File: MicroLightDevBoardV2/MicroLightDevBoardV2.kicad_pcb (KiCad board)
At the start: 2 copper layers, 80.4 x 72.6 mm, 65 parts, among them J1 Conn_01x05_Socket, J10 Conn_01x01_Socket, J11 Conn_01x05_Socket, J12 Conn_01x02_Socket, J13 Conn_01x04_Socket, J14 Conn_01x04_Socket, J15 Conn_01x05_Socket, J16 Conn_01x01_Socket, J17 Conn_01x04_Socket, J18 Conn_01x04_Socket, J19 Conn_01x04_Socket, J2 Conn_01x05_Socket, J20 Conn_01x04_Socket, J21 Conn_01x04_Socket, J22 Conn_01x04_Socket, J23 Conn_01x03_Socket, J24 Conn_01x03_Socket, J25 Conn_01x04_Socket, J26 Conn_01x04_Socket, J27 Conn_01x02_Socket, J28 Conn_01x02_Socket, J29 Conn_01x02_Socket, J3 Conn_01x05_Socket, J30 Conn_01x02_Socket, J31 Conn_01x01_Socket, J32 Conn_01x06_Socket, J33 Conn_01x04_Socket, J4 Conn_01x05_Socket, J5 Conn_01x02_Socket, J6 Conn_01x02_Socket, J7 TYPE-C-31-M-12, J8 Conn_01x02_Socket, J9 Conn_01x02_Socket, U1 BQ25628RYKR, U2 ATtiny3226-M, U3 S-85S1AB33-I6T1U, U4 USBLC6-2P6, U5 MC3479

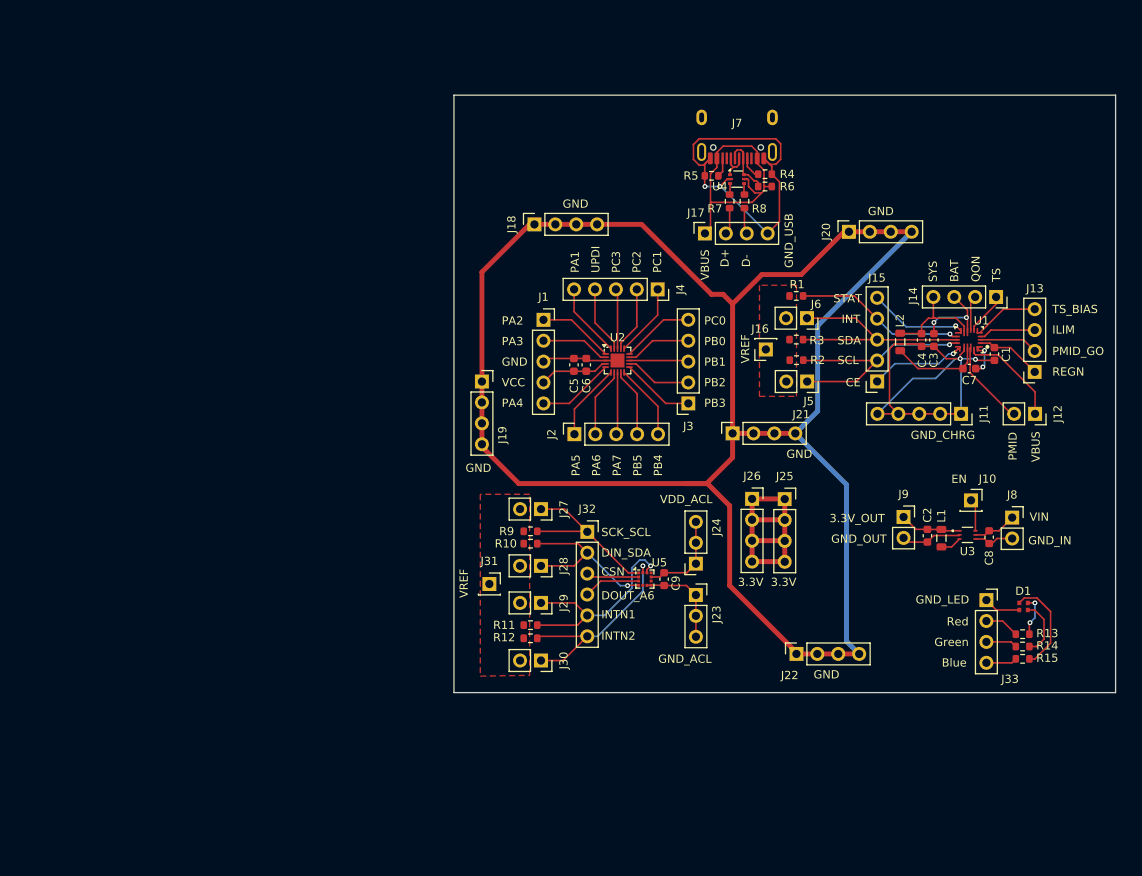
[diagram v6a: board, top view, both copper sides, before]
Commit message: add buttons to pcb, add breadboard like expansion sockets
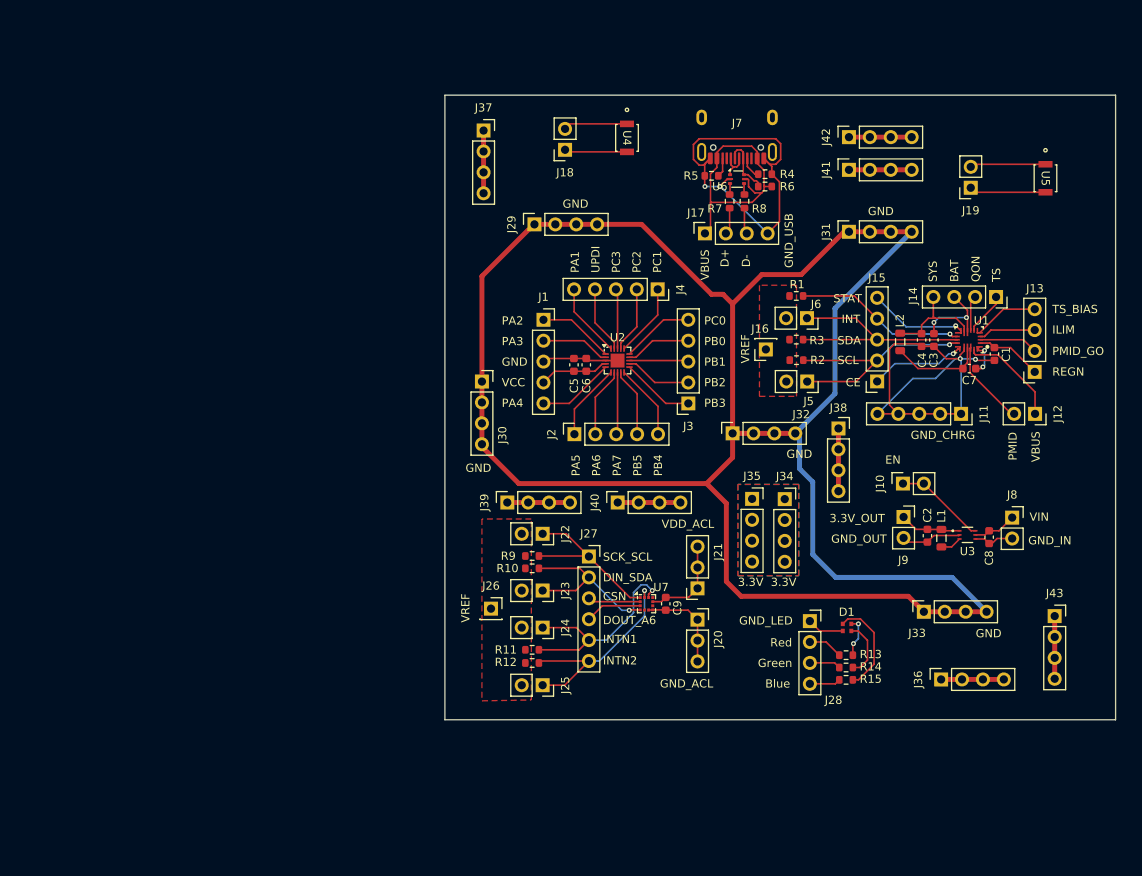
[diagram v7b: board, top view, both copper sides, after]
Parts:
- added J18: Conn_01x02_Socket, Connector_PinSocket_2.54mm:PinSocket_1x02_P2.54mm_Vertical, F.Cu at (132.8, 43.4)
- added J19: Conn_01x02_Socket, Connector_PinSocket_2.54mm:PinSocket_1x02_P2.54mm_Vertical, F.Cu at (182.1, 48.0)
- added J36: Conn_01x04_Socket, Connector_PinSocket_2.54mm:PinSocket_1x04_P2.54mm_Vertical, F.Cu at (178.5, 107.8)
- added J37: Conn_01x04_Socket, Connector_PinSocket_2.54mm:PinSocket_1x04_P2.54mm_Vertical, F.Cu at (122.9, 41.1)
- added J38: Conn_01x04_Socket, Connector_PinSocket_2.54mm:PinSocket_1x04_P2.54mm_Vertical, F.Cu at (166.0, 77.3)
- added J39: Conn_01x04_Socket, Connector_PinSocket_2.54mm:PinSocket_1x04_P2.54mm_Vertical, F.Cu at (125.8, 86.3)
- added J40: Conn_01x04_Socket, Connector_PinSocket_2.54mm:PinSocket_1x04_P2.54mm_Vertical, F.Cu at (139.2, 86.3)
- added J41: Conn_01x04_Socket, Connector_PinSocket_2.54mm:PinSocket_1x04_P2.54mm_Vertical, F.Cu at (167.3, 45.9)
- added J42: Conn_01x04_Socket, Connector_PinSocket_2.54mm:PinSocket_1x04_P2.54mm_Vertical, F.Cu at (167.3, 41.9)
- added J43: Conn_01x04_Socket, Connector_PinSocket_2.54mm:PinSocket_1x04_P2.54mm_Vertical, F.Cu at (192.3, 100.1)
- added U4: B3U-1000P, MicroLightDevBoard:B3U-1000P, F.Cu at (140.3, 42.0)
- added U5: B3U-1000P, MicroLightDevBoard:B3U-1000P, F.Cu at (191.2, 46.9)
- J10: value Conn_01x01_Socket -> Conn_01x02_Socket; footprint Connector_PinSocket_2.54mm:PinSocket_1x01_P2.54mm_Vertical -> Connector_PinSocket_2.54mm:PinSocket_1x02_P2.54mm_Vertical
- moved D1 21.6 mm to (167.1, 101.5)
- moved R13 21.6 mm to (166.9, 104.8)
- moved R14 21.6 mm to (166.9, 106.3)
- moved R15 21.6 mm to (166.9, 107.8)
- moved J28 21.6 mm to (162.6, 100.7)
- moved J33 16.3 mm to (176.4, 99.6)
- moved J10 8.52 mm to (173.9, 84.0), turned to 90 degrees
- moved J20 3.01 mm to (148.9, 100.5)
- moved J21 3.01 mm to (148.9, 96.7)
- moved R10 3.01 mm to (128.8, 94.3)
- moved R11 3.01 mm to (128.8, 104.2)
- moved R12 3.01 mm to (128.8, 105.8)
- moved R9 3.01 mm to (128.8, 92.8)
- moved J26 3.01 mm to (123.8, 99.2)
- moved C9 3.01 mm to (145.0, 98.6)
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- renumbered J23 to J20, J24 to J21, J27 to J22, J28 to J23, J29 to J24, J30 to J25, J31 to J26, J32 to J27, J33 to J28, J18 to J29, J19 to J30, J20 to J31, J21 to J32, J22 to J33, J25 to J34, J26 to J35, U4 to U6, U5 to U7
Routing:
- net 3.3V_LANE: track 31.2 -> 0.07 mm
- net GND_LANE: track 239.2 -> 259.1 mm
- net Button2B: track 0.00 -> 9.31 mm
- net Button2A: track 0.00 -> 9.21 mm
- net Button1A: track 0.00 -> 7.78 mm
- net Button1B: track 0.00 -> 7.63 mm
- net Net-(J43-Pin_1): track 0.00 -> 7.62 mm
- net Net-(J40-Pin_1): track 0.00 -> 7.62 mm
- net Net-(J39-Pin_1): track 0.00 -> 7.62 mm
- net Net-(J38-Pin_1): track 0.00 -> 7.62 mm
- net Net-(J36-Pin_1): track 0.00 -> 7.62 mm
- net Net-(J37-Pin_1): track 0.00 -> 7.62 mm
- net Net-(J42-Pin_1): track 0.00 -> 7.62 mm
- net Net-(J41-Pin_1): track 0.00 -> 7.62 mm
- net EN_3V3: track 3.92 -> 11.2 mm
- added copper zone on B.Cu, net 3.3V_LANE
- added copper zone on F.Cu, net 3.3V_LANE
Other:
- board size 80.4 x 72.6 mm -> 81.5 x 75.9 mm

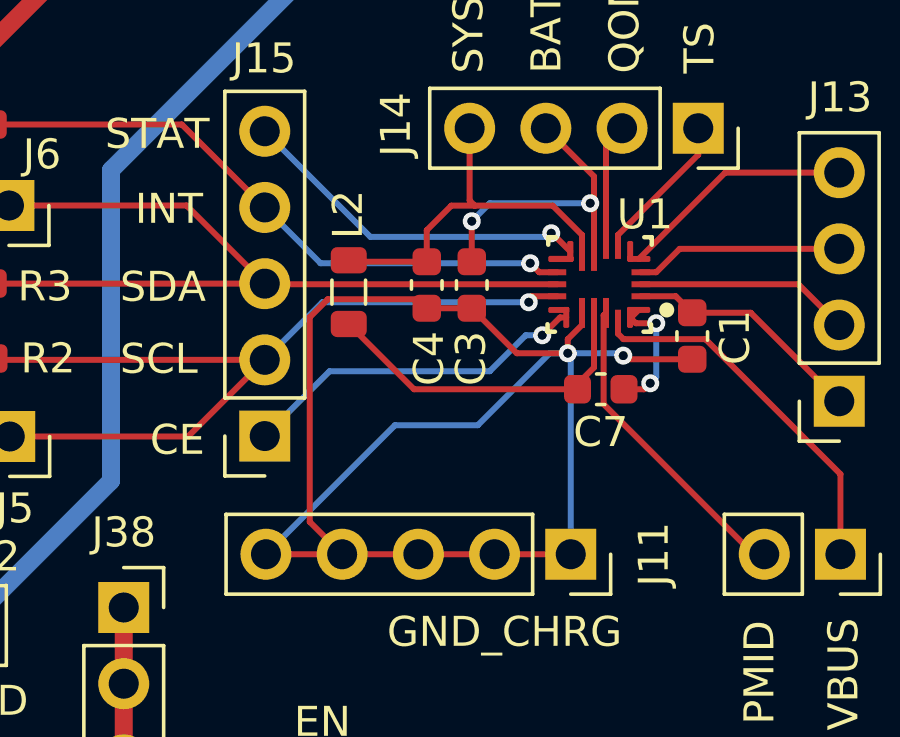
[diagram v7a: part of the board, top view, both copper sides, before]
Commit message: add 1uh power inductor footprint from Wurth Elektronik
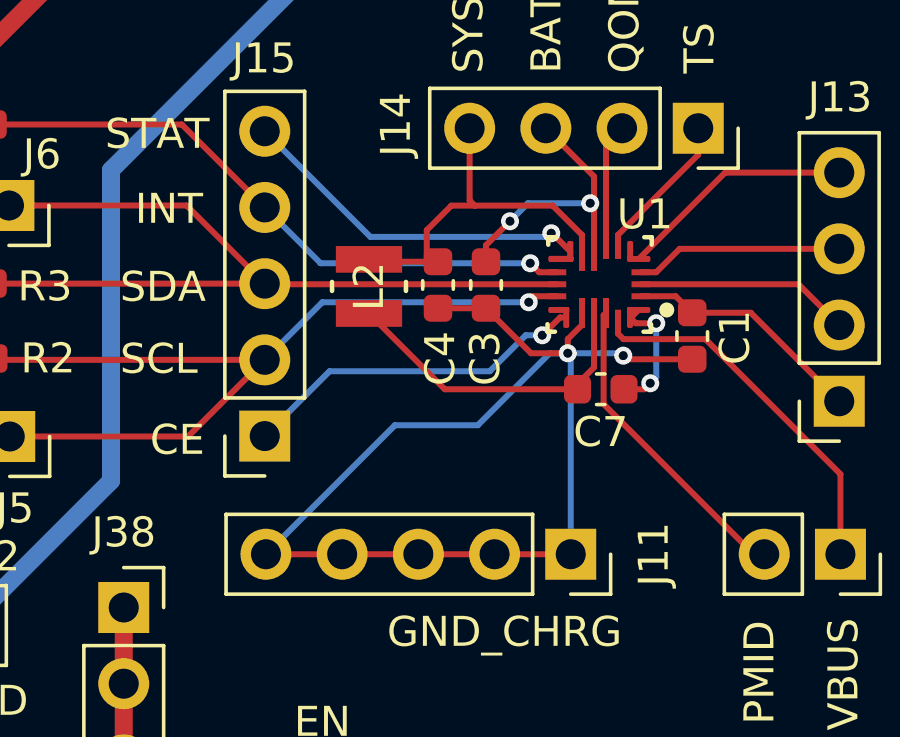
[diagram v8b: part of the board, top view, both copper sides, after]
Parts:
- L2: footprint Inductor_SMD:L_0805_2012Metric -> MicroLightDevBoard:IND_2508-WE-MAPI_WRE
- moved L2 0.70 mm to (174.2, 66.6)
- moved C3 0.47 mm to (178.1, 66.5)
- moved C4 0.38 mm to (176.5, 66.5)
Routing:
- net GND_CHRG: track 53.5 -> 40.5 mm
- net BAT: track 10.6 -> 9.63 mm
- net SW: track 11.4 -> 10.8 mm
